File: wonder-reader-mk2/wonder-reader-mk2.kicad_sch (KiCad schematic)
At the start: 33 parts, among them M1 Stepper_Motor_unipolar_5pin, M2 Stepper_Motor_bipolar, M3 Stepper_Motor_bipolar, M4 Stepper_Motor_bipolar, M5 Stepper_Motor_bipolar, M6 Stepper_Motor_bipolar, M7 Stepper_Motor_bipolar, SW1 SW_Push, SW2 SW_Push, SW3 SW_Push, SW4 SW_Push, SW5 SW_Push, SW6 Stepper_Limit, SW8 SW_SPST, U1 ESP32, U2 MAX98357A, U3 BQ297xy, U3 Vibration Motor, U5 ULN2003, U7 74HC595, U8 74HC595, U9 74HC595

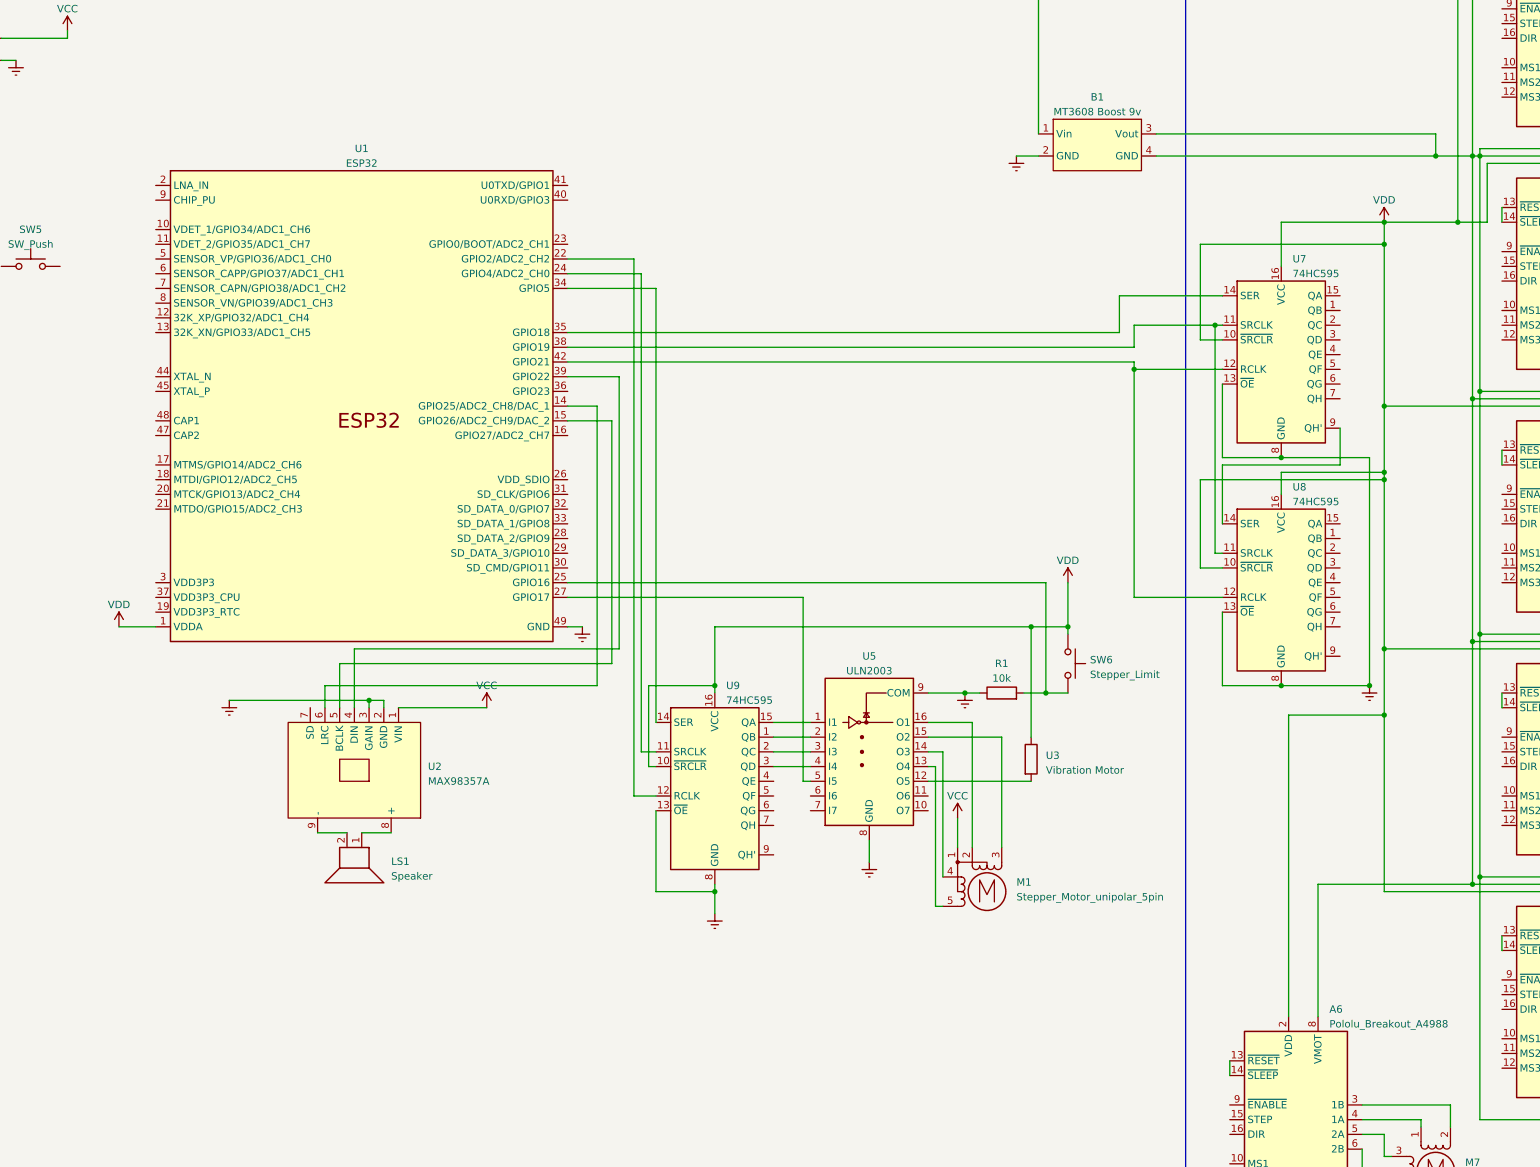
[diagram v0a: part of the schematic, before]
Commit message: Updated cell top height. Carriage load now can be joined together as they have a connecttor. New gearbox for x stepper motor speed. Updated PCB design
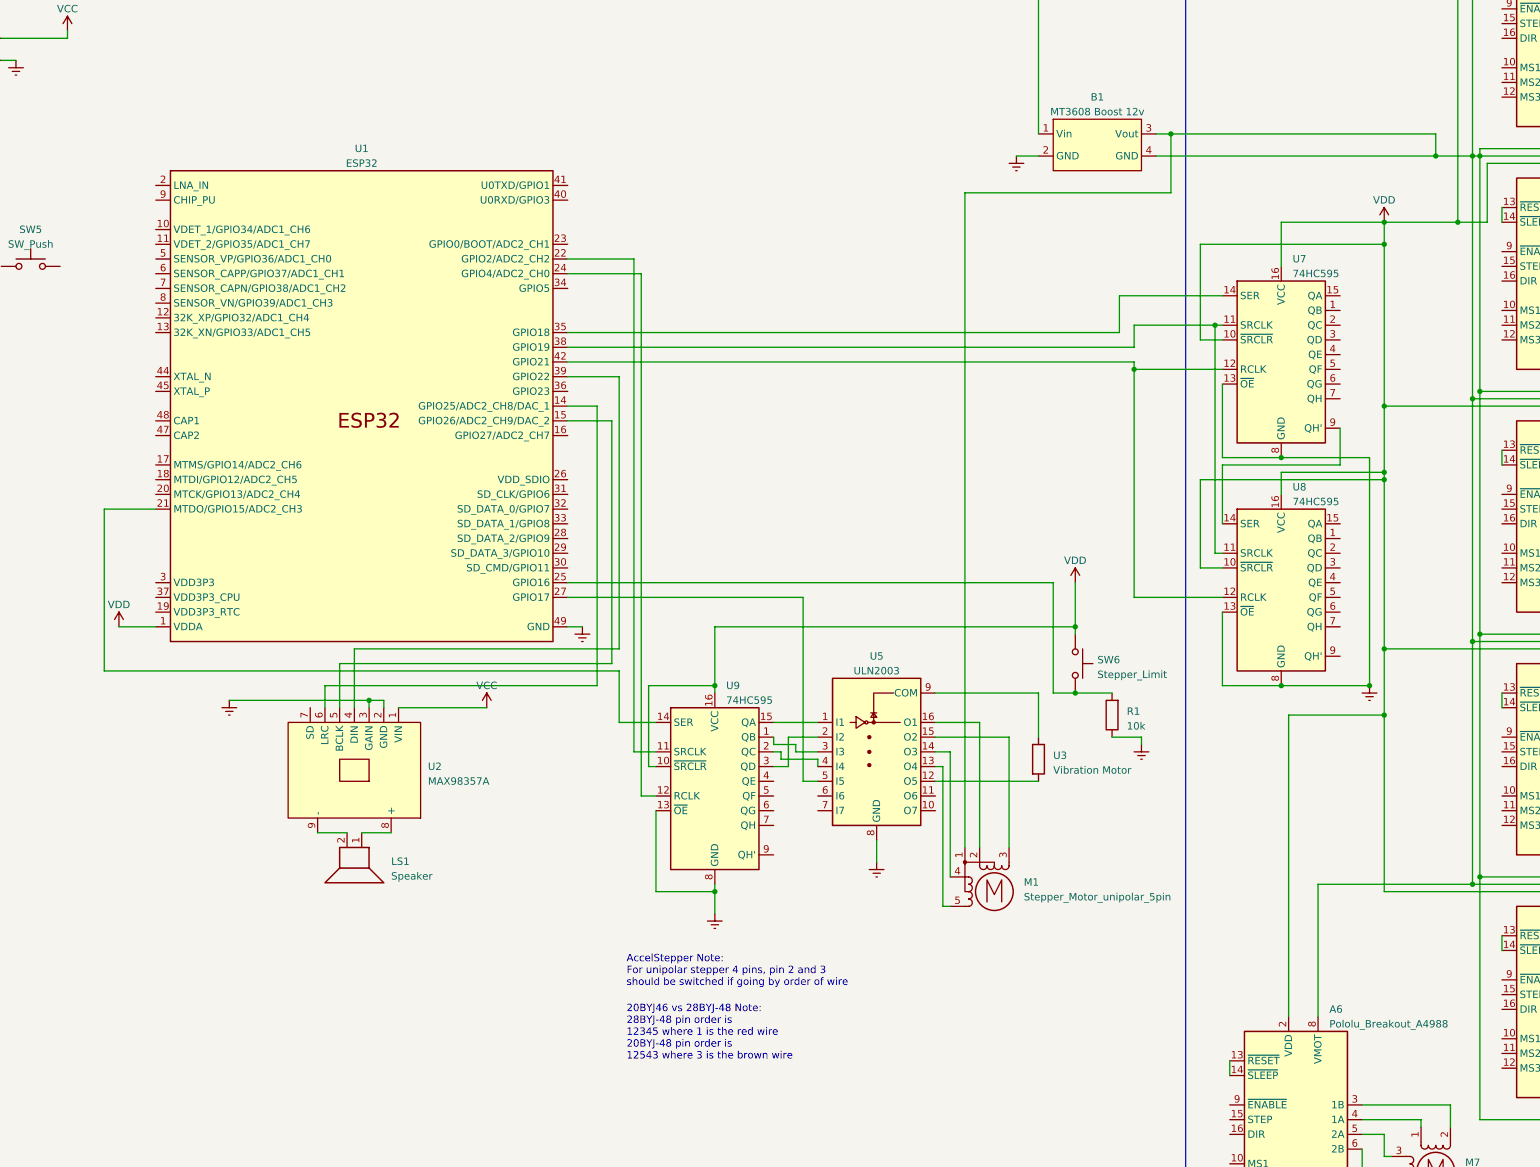
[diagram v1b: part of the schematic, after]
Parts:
- B1: value MT3608 Boost 9v -> MT3608 Boost 12v
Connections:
- net Earth: no longer U5.9 (COM)
- net VCC: no longer M1.1
- net VDD: no longer U3.1
- net at U5.2 (I2): now also U9.3 (QD); no longer U9.1 (QB)
- net at U5.3 (I3): now also U9.1 (QB); no longer U9.2 (QC)
- net at U5.4 (I4): now also U9.2 (QC); no longer U9.3 (QD)
- net at A1.7 (GND), A1.8 (VMOT), A2.7 (GND)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: now also M1.1
- net at U1.21 (MTDO/GPIO15/ADC2_CH3): now also U9.14 (SER)
- net at U1.22 (GPIO2/ADC2_CH2): now also U9.11 (SRCLK); no longer U9.12 (RCLK)
- net at U1.24 (GPIO4/ADC2_CH0): now also U9.12 (RCLK); no longer U9.11 (SRCLK)
- net at U1.34 (GPIO5): no longer U9.14 (SER)
- new net: U3.1, U5.9 (COM)
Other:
- note added: "20BYJ46 vs 28BYJ-48 Note: 28BYJ-48 pin order is 12345 where 1 is the red wire 20BYJ-48 pin order is 12543 where 3 is the brown wire"
- note added: "AccelStepper Note: For unipolar stepper 4 pins, pin 2 and 3 should be switched if going by order of wire"
- moved on the sheet: M1, R1, SW6, U3, U5

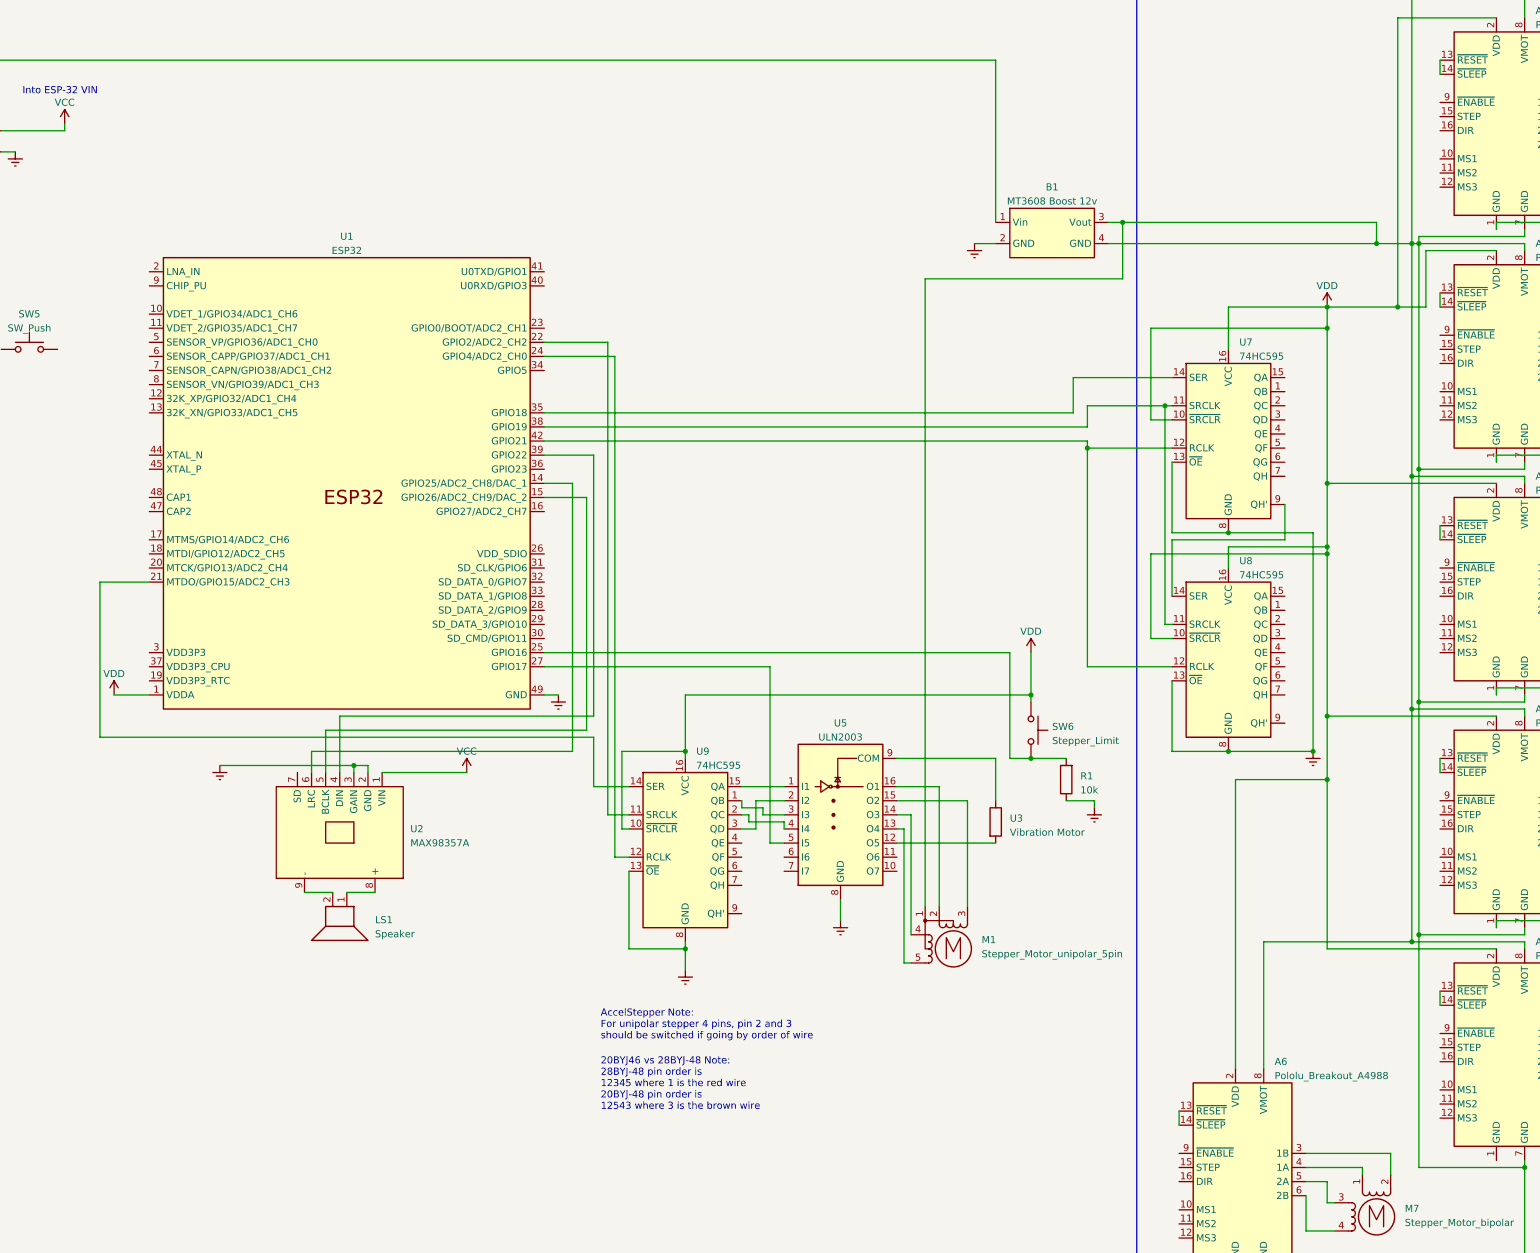
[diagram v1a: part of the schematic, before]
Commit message: New 1:3 gearbox. Bearing bracket start second gear holder not hitting screw
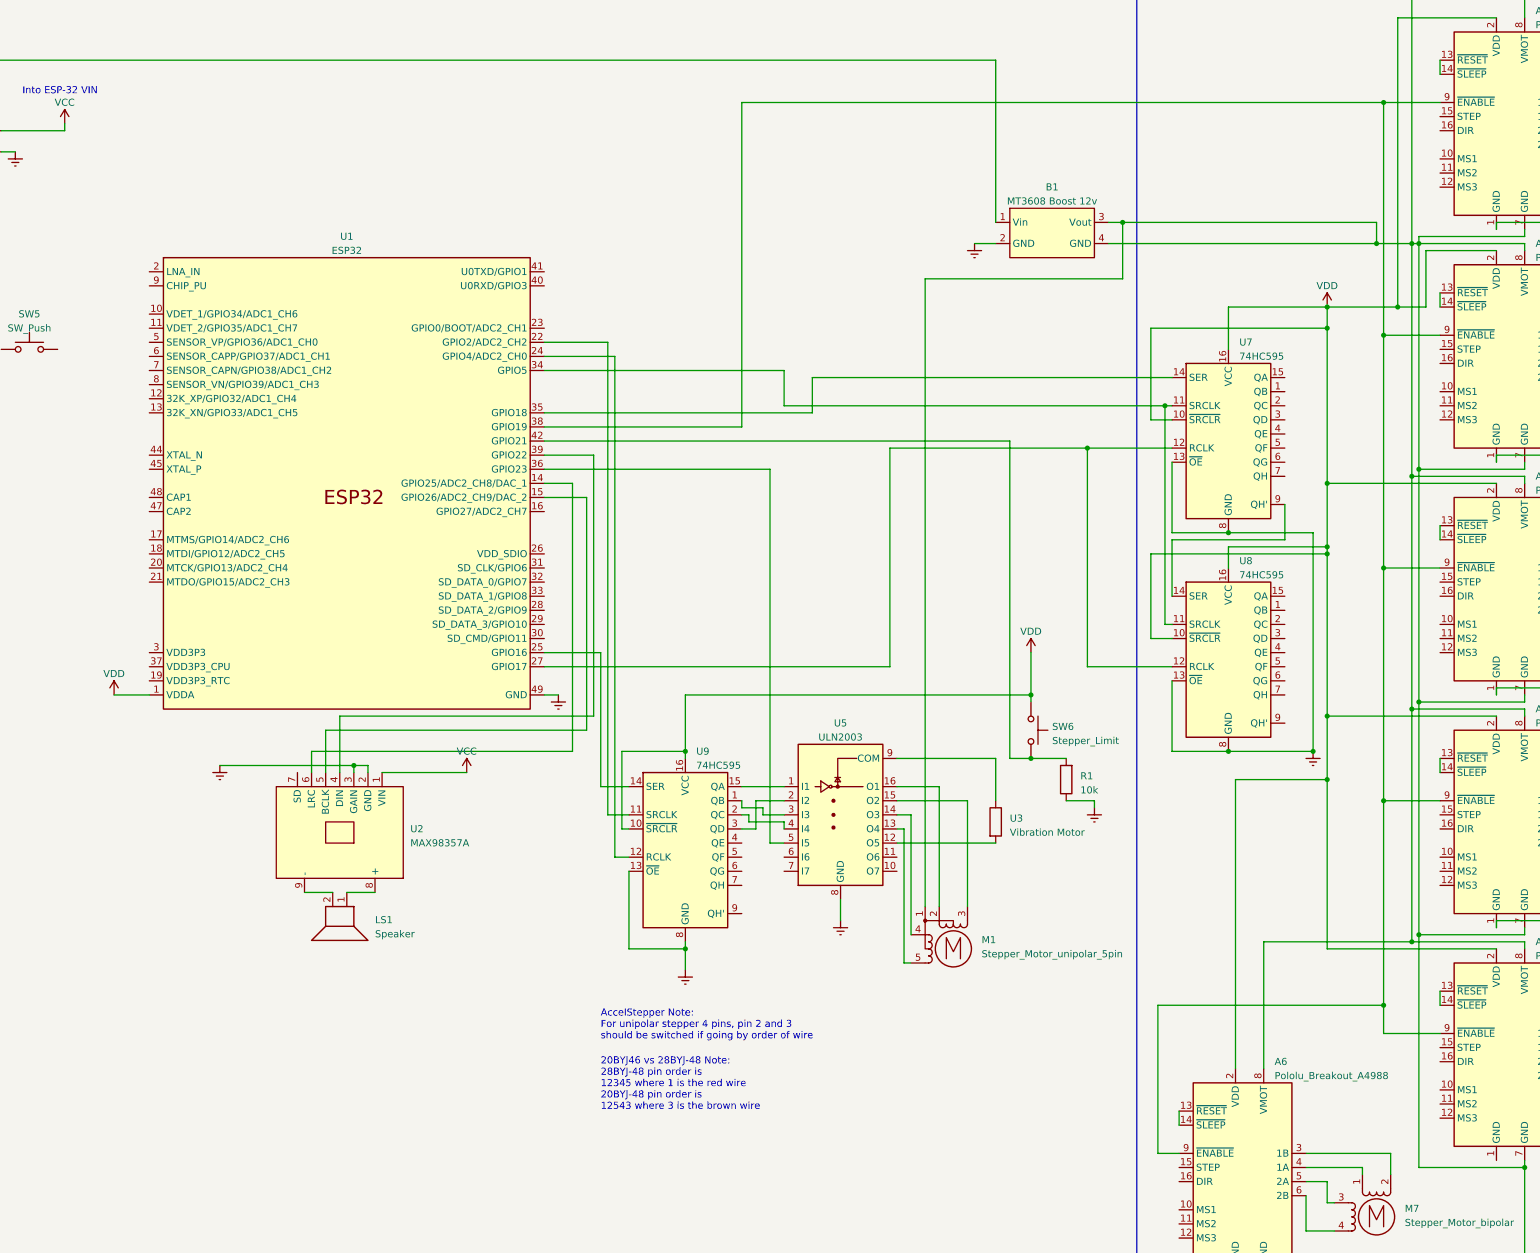
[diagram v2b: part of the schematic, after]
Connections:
- net at U5.5 (I5): now also U1.36 (GPIO23); no longer U1.27 (GPIO17)
- net at U7.11 (SRCLK), U8.11 (SRCLK): now also U1.34 (GPIO5); no longer U1.38 (GPIO19)
- net at U7.12 (RCLK), U8.12 (RCLK): now also U1.27 (GPIO17); no longer U1.42 (GPIO21)
- net at A1.9 (~{ENABLE}): now also A2.9 (~{ENABLE}), A3.9 (~{ENABLE}), A4.9 (~{ENABLE}), A5.9 (~{ENABLE}), A6.9 (~{ENABLE}), U1.38 (GPIO19)
- net at U1.21 (MTDO/GPIO15/ADC2_CH3): no longer U9.14 (SER)
- net at R1.2, SW6.2: now also U1.42 (GPIO21); no longer U1.25 (GPIO16)
- new net: U1.25 (GPIO16), U9.14 (SER)
